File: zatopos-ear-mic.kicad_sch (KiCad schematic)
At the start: 20 parts, among them J2 Conn_01x06_Socket, U1 NJU7043, U2 MCP3002

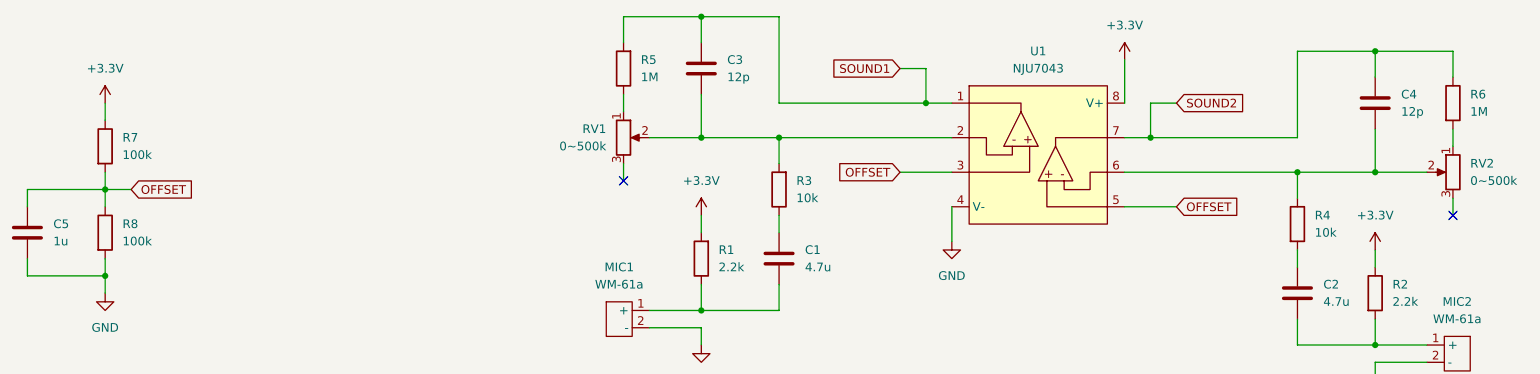
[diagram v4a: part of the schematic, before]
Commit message: Change footprints to JLCPCB basic parts
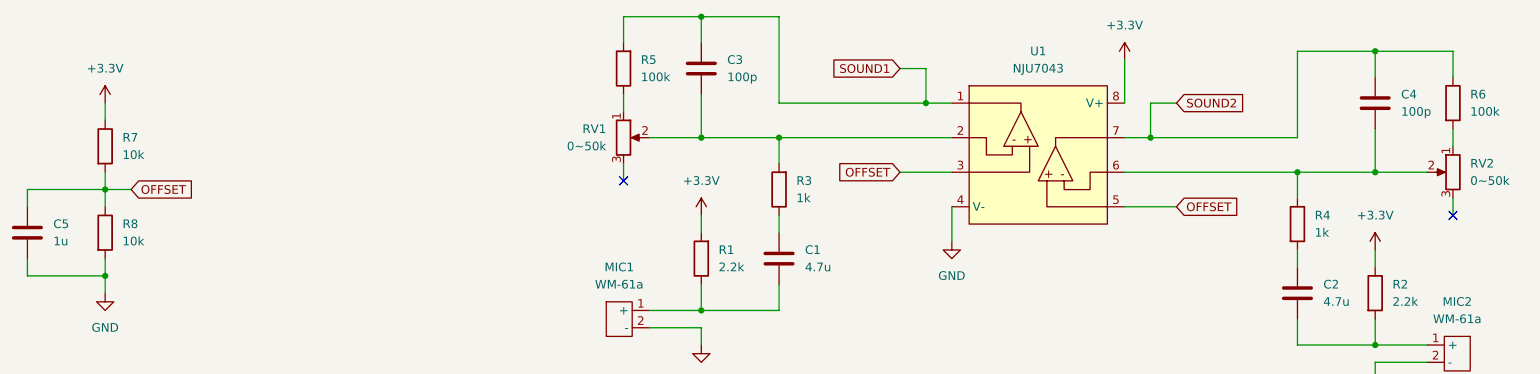
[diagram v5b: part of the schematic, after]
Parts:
- C1, C2: footprint Capacitor_SMD:C_1206_3216Metric -> Capacitor_SMD:C_0603_1608Metric; LCSC PN (none) -> C19666
- C3, C4: value 12p -> 100p; footprint Capacitor_SMD:C_1206_3216Metric -> Capacitor_SMD:C_0603_1608Metric; LCSC PN (none) -> C14858
- C5: footprint Capacitor_SMD:C_1206_3216Metric -> Capacitor_SMD:C_0603_1608Metric; LCSC PN (none) -> C15849
- R1, R2: footprint Resistor_SMD:R_1206_3216Metric -> Resistor_SMD:R_0603_1608Metric; LCSC PN (none) -> C4190
- R3, R4: value 10k -> 1k; footprint Resistor_SMD:R_1206_3216Metric -> Resistor_SMD:R_0603_1608Metric; LCSC PN (none) -> C21190
- R5, R6: value 1M -> 100k; footprint Resistor_SMD:R_1206_3216Metric -> Resistor_SMD:R_0603_1608Metric; LCSC PN (none) -> C25803
- R7, R8: value 100k -> 10k; footprint Resistor_SMD:R_1206_3216Metric -> Resistor_SMD:R_0603_1608Metric; LCSC PN (none) -> C25804
- RV1, RV2: value 0~500k -> 0~50k
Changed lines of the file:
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@@
 			)
 		)
-		(property "Value" "10k"
+		(property "Value" "1k"
 			(at 161.29 66.0399 0)
 			(effects
@@
 			)
 		)
-		(property "Footprint" "Resistor_SMD:R_1206_3216Metric"
+		(property "Footprint" "Resistor_SMD:R_0603_1608Metric"
 			(at 160.528 64.77 90)
 			(effects
@@
 		)
 		(property "Description" "Resistor"
+			(at 158.75 64.77 0)
+			(effects
+				(font
+					(size 1.27 1.27)
+				)
+				(hide yes)
+			)
+		)
+		(property "LCSC PN" "C21190"
 			(at 158.75 64.77 0)
 			(effects
@@
 			)
 		)
+		(property "LCSC PN" ""
+			(at 135.89 83.82 0)
+			(effects
+				(font
+					(size 1.27 1.27)
+				)
+				(hide yes)
+			)
+		)
 		(pin "2"
 		)
@@
 			)
 		)
-		(property "Value" "12p"
+		(property "Value" "100p"
 			(at 151.13 48.2599 0)
 			(effects
@@
 			)
 		)
-		(property "Footprint" "Capacitor_SMD:C_1206_3216Metric"
+		(property "Footprint" "Capacitor_SMD:C_0603_1608Metric"
 			(at 148.2852 50.8 0)
 			(effects
@@
 		)
 		(property "Description" "Unpolarized capacitor"
+			(at 147.32 46.99 0)
+			(effects
+				(font
+					(size 1.27 1.27)
+				)
+				(hide yes)
+			)
+		)
+		(property "LCSC PN" "C14858"
 			(at 147.32 46.99 0)
 			(effects
@@
 			)
 		)
+		(property "LCSC PN" ""
+			(at 257.81 88.9 0)
+			(effects
+				(font
+					(size 1.27 1.27)
+				)
+				(hide yes)
+			)
+		)
 		(pin "1"
 		)
@@
 			)
 		)
-		(property "Value" "0~500k"
+		(property "Value" "0~50k"
 			(at 260.35 63.4999 0)
 			(effects
@@
 			)
 		)
+		(property "LCSC PN" ""
+			(at 257.81 62.23 0)
+			(effects
+				(font
+					(size 1.27 1.27)
+				)
+				(hide yes)
+			)
+		)
 		(pin "3"
 		)
@@
 			)
 		)
-		(property "Footprint" "Resistor_SMD:R_1206_3216Metric"
+		(property "Footprint" "Resistor_SMD:R_0603_1608Metric"
 			(at 149.098 74.93 90)
 			(effects
@@
 			)
 		)
+		(property "LCSC PN" "C4190"
+			(at 147.32 74.93 0)
+			(effects
+				(font
+					(size 1.27 1.27)
+				)
+				(hide yes)
+			)
+		)
 		(pin "1"
 		)
@@
 			)
 		)
-		(property "Footprint" "Resistor_SMD:R_1206_3216Metric"
+		(property "Footprint" "Resistor_SMD:R_0603_1608Metric"
 			(at 244.602 80.01 90)
 			(effects
@@
 			)
 		)
+		(property "LCSC PN" "C4190"
+			(at 246.38 80.01 0)
+			(effects
+				(font
+					(size 1.27 1.27)
+				)
+				(hide yes)
+			)
+		)
 		(pin "2"
 		)
@@
 			)
 		)
-		(property "Value" "1M"
+		(property "Value" "100k"
 			(at 260.35 53.3399 0)
 			(effects
@@
 			)
 		)
-		(property "Footprint" "Resistor_SMD:R_1206_3216Metric"
+		(property "Footprint" "Resistor_SMD:R_0603_1608Metric"
 			(at 256.032 52.07 90)
 			(effects
@@
 			)
 		)
+		(property "LCSC PN" "C25803"
+			(at 257.81 52.07 0)
+			(effects
+				(font
+					(size 1.27 1.27)
+				)
+				(hide yes)
+			)
+		)
 		(pin "1"
 		)
@@
 			)
 		)
-		(property "Value" "100k"
+		(property "Value" "10k"
 			(at 62.23 59.6899 0)
 			(effects
@@
 			)
 		)
-		(property "Footprint" "Resistor_SMD:R_1206_3216Metric"
+		(property "Footprint" "Resistor_SMD:R_0603_1608Metric"
 			(at 57.912 58.42 90)
 			(effects
@@
 			)
 		)
+		(property "LCSC PN" "C25804"
+			(at 59.69 58.42 0)
+			(effects
+				(font
+					(size 1.27 1.27)
+				)
+				(hide yes)
+			)
+		)
 		(pin "2"
 		)
@@
 			)
 		)
-		(property "Footprint" "Capacitor_SMD:C_1206_3216Metric"
+		(property "Footprint" "Capacitor_SMD:C_0603_1608Metric"
 			(at 159.7152 78.74 0)
 			(effects
@@
 			)
 		)
+		(property "LCSC PN" "C19666"
+			(at 158.75 74.93 0)
+			(effects
+				(font
+					(size 1.27 1.27)
+				)
+				(hide yes)
+			)
+		)
 		(pin "2"
 		)
@@
 			)
 		)
+		(property "LCSC PN" ""
+			(at 80.01 149.86 0)
+			(effects
+				(font
+					(size 1.27 1.27)
+				)
+				(hide yes)
+			)
+		)
 		(pin "7"
 		)
@@
 			)
 		)
-		(property "Value" "12p"
+		(property "Value" "100p"
 			(at 250.19 53.3399 0)
 			(effects
@@
 			)
 		)
-		(property "Footprint" "Capacitor_SMD:C_1206_3216Metric"
+		(property "Footprint" "Capacitor_SMD:C_0603_1608Metric"
 			(at 247.3452 55.88 0)
 			(effects
@@
 			)
 		)
+		(property "LCSC PN" "C14858"
+			(at 246.38 52.07 0)
+			(effects
+				(font
+					(size 1.27 1.27)
+				)
+				(hide yes)
+			)
+		)
 		(pin "2"
 		)
@@
 			)
 		)
-		(property "Footprint" "Capacitor_SMD:C_1206_3216Metric"
+		(property "Footprint" "Capacitor_SMD:C_0603_1608Metric"
 			(at 235.9152 83.82 0)
 			(effects
@@
 			)
 		)
+		(property "LCSC PN" "C19666"
+			(at 234.95 80.01 0)
+			(effects
+				(font
+					(size 1.27 1.27)
+				)
+				(hide yes)
+			)
+		)
 		(pin "2"
 		)
@@
 			)
 		)
+		(property "LCSC PN" ""
+			(at 196.85 59.69 0)
+			(effects
+				(font
+					(size 1.27 1.27)
+				)
+				(hide yes)
+			)
+		)
 		(pin "3"
 		)
@@
 			)
 		)
-		(property "Value" "1M"
+		(property "Value" "100k"
 			(at 138.43 48.2599 0)
 			(effects
@@
 			)
 		)
-		(property "Footprint" "Resistor_SMD:R_1206_3216Metric"
+		(property "Footprint" "Resistor_SMD:R_0603_1608Metric"
 			(at 137.668 46.99 90)
 			(effects
@@
 			)
 		)
+		(property "LCSC PN" "C25803"
+			(at 135.89 46.99 0)
+			(effects
+				(font
+					(size 1.27 1.27)
+				)
+				(hide yes)
+			)
+		)
 		(pin "2"
 		)
@@
 			)
 		)
-		(property "Footprint" "Capacitor_SMD:C_1206_3216Metric"
+		(property "Footprint" "Capacitor_SMD:C_0603_1608Metric"
 			(at 49.2252 74.93 0)
 			(effects
@@
 		)
 		(property "Description" "Unpolarized capacitor"
+			(at 48.26 71.12 0)
+			(effects
+				(font
+					(size 1.27 1.27)
+				)
+				(hide yes)
+			)
+		)
+		(property "LCSC PN" "C15849"
 			(at 48.26 71.12 0)
 			(effects
@@
 			)
 		)
+		(property "LCSC PN" ""
+			(at 120.65 151.13 0)
+			(effects
+				(font
+					(size 1.27 1.27)
+				)
+				(hide yes)
+			)
+		)
 		(pin "5"
 		)
@@
 			)
 		)
-		(property "Value" "0~500k"
+		(property "Value" "0~50k"
 			(at 133.35 58.4199 0)
 			(effects
@@
 			)
 		)
+		(property "LCSC PN" ""
+			(at 135.89 57.15 0)
+			(effects
+				(font
+					(size 1.27 1.27)
+				)
+				(hide yes)
+			)
+		)
 		(pin "2"
 		)
@@
 			)
 		)
-		(property "Value" "100k"
+		(property "Value" "10k"
 			(at 62.23 72.3899 0)
 			(effects
@@
 			)
 		)
-		(property "Footprint" "Resistor_SMD:R_1206_3216Metric"
+		(property "Footprint" "Resistor_SMD:R_0603_1608Metric"
 			(at 57.912 71.12 90)
 			(effects
@@
 			)
 		)
+		(property "LCSC PN" "C25804"
+			(at 59.69 71.12 0)
+			(effects
+				(font
+					(size 1.27 1.27)
+				)
+				(hide yes)
+			)
+		)
 		(pin "2"
 		)
@@
 			)
 		)
-		(property "Value" "10k"
+		(property "Value" "1k"
 			(at 237.49 71.1199 0)
 			(effects
@@
 			)
 		)
-		(property "Footprint" "Resistor_SMD:R_1206_3216Metric"
+		(property "Footprint" "Resistor_SMD:R_0603_1608Metric"
 			(at 233.172 69.85 90)
 			(effects
@@
 			(at 234.95 69.85 0)
 			(effects
+				(font
+					(size 1.27 1.27)
+				)
+				(hide yes)
+			)
+		)
+		(property "LCSC PN" "C21190"
+			(at 234.95 69.85 0)
+			(effects
